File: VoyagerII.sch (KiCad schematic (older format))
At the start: 20 parts, among them P1 TC2030-IDC, SW1 SW_PUSH, U1 ATXMEGA32A4U-AU, U2 MCP1700T-3002E/TT, U3 STF202-22T1G, U4 IS31FL3731-SALS2

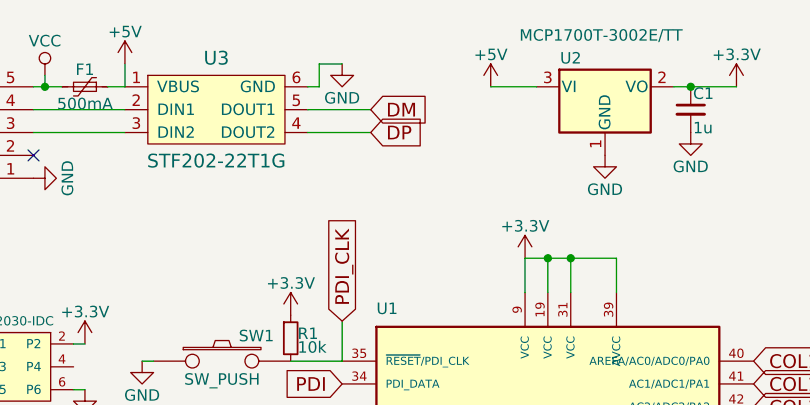
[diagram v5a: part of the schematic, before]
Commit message: Fix USB net name
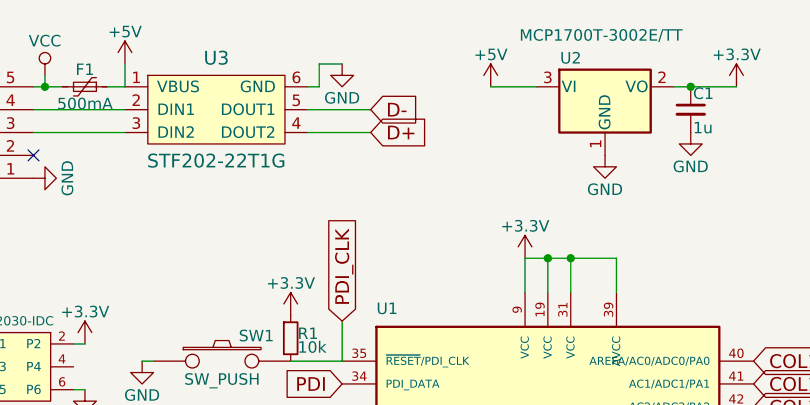
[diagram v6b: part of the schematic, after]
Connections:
- net DM is gone; now on net D-: U3.5 (DOUT1)
- net DP is gone; now on net D+: U3.4 (DOUT2)
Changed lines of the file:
@@
 	0    -1   -1   0
 $EndComp
-Text GLabel 2900 1500 2    60   Input ~ 0
-DP
-Text GLabel 2900 1400 2    60   Input ~ 0
-DM
 $Comp
 L Polyfuse_Small F1
@@
 Text GLabel 7325 4350 2    60   Input ~ 0
 LED-B9
+Text GLabel 2900 1400 2    60   Input ~ 0
+D-
+Text GLabel 2900 1500 2    60   Input ~ 0
+D+
 $EndSCHEMATC

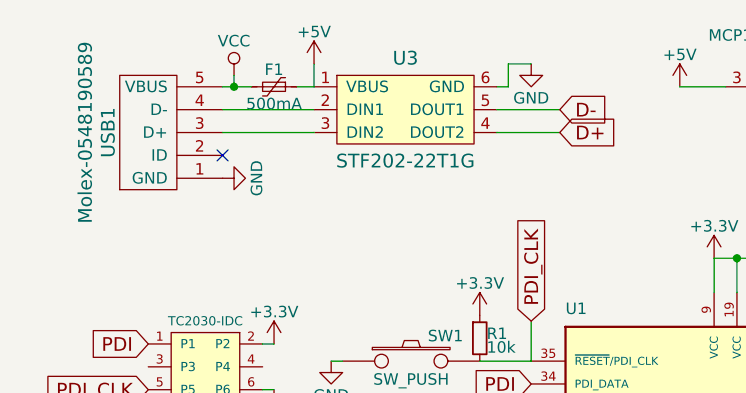
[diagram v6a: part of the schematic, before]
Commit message: Break out controller a bit
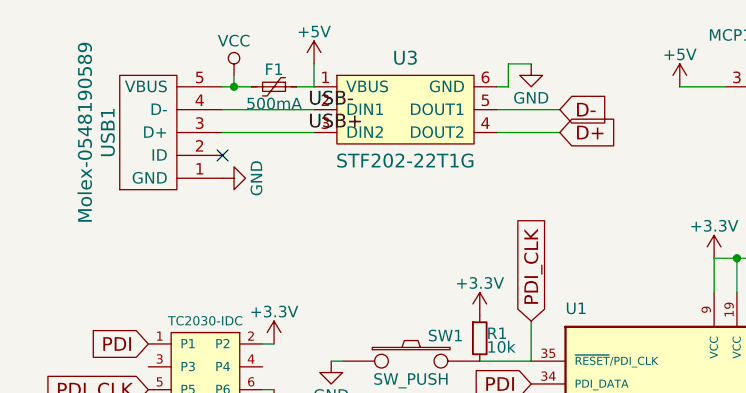
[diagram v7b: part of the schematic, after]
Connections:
- net USB+: now reaches U3.3 (DIN2), USB1.3 (D+)
- net USB-: now reaches U3.2 (DIN1), USB1.4 (D-)
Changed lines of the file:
@@
 Text GLabel 2900 1500 2    60   Input ~ 0
 D+
+Text Label 1800 1400 0    60   ~ 0
+USB-
+Text Label 1800 1500 0    60   ~ 0
+USB+
 $EndSCHEMATC
